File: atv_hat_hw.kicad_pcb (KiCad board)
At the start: 2 copper layers, 84.1 x 83.9 mm, 51 parts, among them J1 GPIO_CONNECTOR, J10 conn_01x02_labeled, J11 conn_01x02_labeled, J12 conn_01x02_labeled, J2 conn_01x02_labeled, J3 conn_01x02_labeled, J4 conn_01x02_labeled, J5 conn_01x02_labeled, J6 conn_01x02_labeled, J7 enc28j60_hanrun, J8 conn_01x02_labeled, J9 conn_01x02_labeled, Q1 Q_NMOS_GDS, Q2 Q_NMOS_GDS, Q3 Q_NMOS_GDS, Q4 Q_NMOS_GDS, Q5 Q_NMOS_GDS, Q6 Q_NMOS_GDS, Q7 Q_NMOS_GDS, Q8 Q_NMOS_GDS, Q9 Q_NMOS_GDS

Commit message: plus board ready for routing
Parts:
- removed D7, D8: Green, LED_SMD:LED_1206_3216Metric_Pad1.42x1.75mm_HandSolder
- removed the H4 at (90.6, 129.6)
- added C10: 10u, Capacitor_SMD:C_1206_3216Metric_Pad1.42x1.75mm_HandSolder, F.Cu at (80.0, 107.9)
- added C11: 100n, Capacitor_SMD:C_1206_3216Metric_Pad1.42x1.75mm_HandSolder, F.Cu at (90.6, 37.8)
- added C12: 30p, Capacitor_SMD:C_1206_3216Metric_Pad1.42x1.75mm_HandSolder, F.Cu at (86.0, 43.3)
- added C13: 30p, Capacitor_SMD:C_1206_3216Metric_Pad1.42x1.75mm_HandSolder, F.Cu at (90.6, 34.5)
- added C14: 10u, Capacitor_SMD:C_1206_3216Metric_Pad1.42x1.75mm_HandSolder, F.Cu at (80.1, 46.6)
- added C15: 100n, Capacitor_SMD:C_1206_3216Metric_Pad1.42x1.75mm_HandSolder, F.Cu at (99.2, 24.6)
- added C16: 100n, Capacitor_SMD:C_1206_3216Metric_Pad1.42x1.75mm_HandSolder, F.Cu at (90.6, 31.2)
- added C17: 10u, Capacitor_SMD:C_1206_3216Metric_Pad1.42x1.75mm_HandSolder, F.Cu at (93.2, 27.9)
- added C3: 100n, Capacitor_SMD:C_1206_3216Metric_Pad1.42x1.75mm_HandSolder, F.Cu at (82.4, 66.4)
- added C4: 10u, Capacitor_SMD:C_1206_3216Metric_Pad1.42x1.75mm_HandSolder, F.Cu at (78.7, 61.8)
- added C5: 100n, Capacitor_SMD:C_1206_3216Metric_Pad1.42x1.75mm_HandSolder, F.Cu at (96.0, 75.4)
- added C6: 10u, Capacitor_SMD:C_1206_3216Metric_Pad1.42x1.75mm_HandSolder, F.Cu at (95.5, 84.3)
- added C7: 100n, Capacitor_SMD:C_1206_3216Metric_Pad1.42x1.75mm_HandSolder, F.Cu at (97.8, 98.4)
- added C8: 10u, Capacitor_SMD:C_1206_3216Metric_Pad1.42x1.75mm_HandSolder, F.Cu at (98.0, 93.1)
- added C9: 100n, Capacitor_SMD:C_1206_3216Metric_Pad1.42x1.75mm_HandSolder, F.Cu at (80.0, 110.2)
- added FB1: 80mA, Inductor_SMD:L_1206_3216Metric_Pad1.42x1.75mm_HandSolder, F.Cu at (80.1, 43.3)
- added H1: MountingHole, lib:MountingHole_2.7mm_M2.5_uHAT_RPi, F.Cu at (106.3, 23.3)
- added J0: phoenix_1935161, lib:PHOENIX_1935161, F.Cu at (106.0, 64.6)
- added J13: phoenix_1935161, lib:PHOENIX_1935161, F.Cu at (245.1, 64.6)
- added J14: phoenix_1935161, lib:PHOENIX_1935161, F.Cu at (255.8, 64.6)
- added J15: phoenix_1935161, lib:PHOENIX_1935161, F.Cu at (266.4, 64.6)
- added J16: phoenix_1935161, lib:PHOENIX_1935161, F.Cu at (103.8, 81.2)
- added J17: phoenix_1935161, lib:PHOENIX_1935161, F.Cu at (114.9, 81.2)
- added J18: phoenix_1935161, lib:PHOENIX_1935161, F.Cu at (125.6, 81.2)
- added J19: phoenix_1935161, lib:PHOENIX_1935161, F.Cu at (136.3, 81.2)
- added J20: phoenix_1935161, lib:PHOENIX_1935161, F.Cu at (147.2, 81.2)
- added J21: phoenix_1935161, lib:PHOENIX_1935161, F.Cu at (157.9, 81.2)
- added J22: phoenix_1935161, lib:PHOENIX_1935161, F.Cu at (168.5, 81.2)
- added J23: phoenix_1935161, lib:PHOENIX_1935161, F.Cu at (179.5, 81.2)
- added J24: phoenix_1935161, lib:PHOENIX_1935161, F.Cu at (190.4, 81.2)
- added J25: phoenix_1935161, lib:PHOENIX_1935161, F.Cu at (201.3, 81.2)
- added J26: phoenix_1935161, lib:PHOENIX_1935161, F.Cu at (212.2, 81.2)
- added J27: phoenix_1935161, lib:PHOENIX_1935161, F.Cu at (222.9, 81.2)
- added J28: phoenix_1935161, lib:PHOENIX_1935161, F.Cu at (233.8, 81.2)
- added J29: phoenix_1935161, lib:PHOENIX_1935161, F.Cu at (244.5, 81.2)
- added J30: phoenix_1935161, lib:PHOENIX_1935161, F.Cu at (255.1, 81.2)
- added J31: phoenix_1935161, lib:PHOENIX_1935161, F.Cu at (265.8, 81.2)
- added J32: phoenix_1935161, lib:PHOENIX_1935161, F.Cu at (105.3, 97.5)
- added J33: phoenix_1935161, lib:PHOENIX_1935161, F.Cu at (116.0, 97.5)
- added J34: phoenix_1935161, lib:PHOENIX_1935161, F.Cu at (126.6, 97.5)
- added J35: phoenix_1935161, lib:PHOENIX_1935161, F.Cu at (137.3, 97.5)
- added J36: phoenix_1935161, lib:PHOENIX_1935161, F.Cu at (148.0, 97.5)
- added J37: phoenix_1935161, lib:PHOENIX_1935161, F.Cu at (158.6, 97.5)
- added J38: phoenix_1935161, lib:PHOENIX_1935161, F.Cu at (169.3, 97.5)
- added J39: phoenix_1935161, lib:PHOENIX_1935161, F.Cu at (180.0, 97.5)
- added J40: phoenix_1935161, lib:PHOENIX_1935161, F.Cu at (190.6, 97.5)
- added J41: phoenix_1935161, lib:PHOENIX_1935161, F.Cu at (201.3, 97.5)
- added J42: phoenix_1935161, lib:PHOENIX_1935161, F.Cu at (212.0, 97.5)
- added J43: phoenix_1935161, lib:PHOENIX_1935161, F.Cu at (222.6, 97.5)
- added J44: phoenix_1935161, lib:PHOENIX_1935161, F.Cu at (233.3, 97.5)
- added J45: phoenix_1935161, lib:PHOENIX_1935161, F.Cu at (244.0, 97.5)
- added J46: phoenix_1935161, lib:PHOENIX_1935161, F.Cu at (254.6, 97.5)
- added J47: phoenix_1935161, lib:PHOENIX_1935161, F.Cu at (265.3, 97.5)
- added J48: phoenix_1935161, lib:PHOENIX_1935161, F.Cu at (103.5, 117.2)
- added J49: phoenix_1935161, lib:PHOENIX_1935161, F.Cu at (114.2, 117.2)
- added J50: phoenix_1935161, lib:PHOENIX_1935161, F.Cu at (124.8, 117.2)
- added J51: phoenix_1935161, lib:PHOENIX_1935161, F.Cu at (135.5, 117.2)
- added J52: phoenix_1935161, lib:PHOENIX_1935161, F.Cu at (146.2, 117.2)
- added J53: phoenix_1935161, lib:PHOENIX_1935161, F.Cu at (156.8, 117.2)
- added J54: phoenix_1935161, lib:PHOENIX_1935161, F.Cu at (167.5, 117.2)
- added J55: phoenix_1935161, lib:PHOENIX_1935161, F.Cu at (178.2, 117.2)
- added J56: phoenix_1935161, lib:PHOENIX_1935161, F.Cu at (188.8, 117.2)
- added J57: phoenix_1935161, lib:PHOENIX_1935161, F.Cu at (199.5, 117.2)
- added J58: phoenix_1935161, lib:PHOENIX_1935161, F.Cu at (210.2, 117.2)
- added J59: phoenix_1935161, lib:PHOENIX_1935161, F.Cu at (220.9, 117.2)
- added J60: phoenix_1935161, lib:PHOENIX_1935161, F.Cu at (231.5, 117.2)
- added J61: phoenix_1935161, lib:PHOENIX_1935161, F.Cu at (242.3, 117.2)
- added J62: phoenix_1935161, lib:PHOENIX_1935161, F.Cu at (253.0, 117.2)
- added J63: phoenix_1935161, lib:PHOENIX_1935161, F.Cu at (263.7, 117.2)
- added J64: phoenix_1935161, lib:SolderWirePad_1x02_P9.0mm_Drill4.5mm, F.Cu at (56.5, 105.3)
- added J65: GPIO_CONNECTOR, lib:PinSocket_2x20_P2.54mm_Vertical_Centered_Anchor, B.Cu at (135.5, 23.1)
- added P1: RB1-125BAG1A, WIZNET_RB1-125BAG1A, F.Cu at (60.5, 35.1)
- added Q0: Q_NMOS_GSD, Package_TO_SOT_SMD:SOT-23_Handsoldering, F.Cu at (108.6, 58.2)
- added Q10: Q_NMOS_GSD, Package_TO_SOT_SMD:SOT-23_Handsoldering, F.Cu at (215.6, 58.5)
- added Q11: Q_NMOS_GSD, Package_TO_SOT_SMD:SOT-23_Handsoldering, F.Cu at (226.3, 58.5)
- added Q12: Q_NMOS_GSD, Package_TO_SOT_SMD:SOT-23_Handsoldering, F.Cu at (237.0, 58.5)
- added Q13: Q_NMOS_GSD, Package_TO_SOT_SMD:SOT-23_Handsoldering, F.Cu at (247.7, 58.5)
- added Q14: Q_NMOS_GSD, Package_TO_SOT_SMD:SOT-23_Handsoldering, F.Cu at (258.3, 58.5)
- added Q15: Q_NMOS_GSD, Package_TO_SOT_SMD:SOT-23_Handsoldering, F.Cu at (269.0, 58.2)
- added Q16: Q_NMOS_GSD, Package_TO_SOT_SMD:SOT-23_Handsoldering, F.Cu at (106.3, 75.1)
- added Q17: Q_NMOS_GSD, Package_TO_SOT_SMD:SOT-23_Handsoldering, F.Cu at (117.5, 75.1)
- added Q18: Q_NMOS_GSD, Package_TO_SOT_SMD:SOT-23_Handsoldering, F.Cu at (128.1, 75.1)
- added Q19: Q_NMOS_GSD, Package_TO_SOT_SMD:SOT-23_Handsoldering, F.Cu at (138.8, 75.1)
- added Q20: Q_NMOS_GSD, Package_TO_SOT_SMD:SOT-23_Handsoldering, F.Cu at (149.7, 75.1)
- added Q21: Q_NMOS_GSD, Package_TO_SOT_SMD:SOT-23_Handsoldering, F.Cu at (160.4, 75.1)
- added Q22: Q_NMOS_GSD, Package_TO_SOT_SMD:SOT-23_Handsoldering, F.Cu at (171.1, 75.1)
- added Q23: Q_NMOS_GSD, Package_TO_SOT_SMD:SOT-23_Handsoldering, F.Cu at (182.0, 75.1)
- added Q24: Q_NMOS_GSD, Package_TO_SOT_SMD:SOT-23_Handsoldering, F.Cu at (192.9, 74.9)
- added Q25: Q_NMOS_GSD, Package_TO_SOT_SMD:SOT-23_Handsoldering, F.Cu at (203.8, 75.1)
- added Q26: Q_NMOS_GSD, Package_TO_SOT_SMD:SOT-23_Handsoldering, F.Cu at (214.8, 75.1)
- added Q27: Q_NMOS_GSD, Package_TO_SOT_SMD:SOT-23_Handsoldering, F.Cu at (225.4, 75.1)
- added Q28: Q_NMOS_GSD, Package_TO_SOT_SMD:SOT-23_Handsoldering, F.Cu at (236.3, 75.1)
- added Q29: Q_NMOS_GSD, Package_TO_SOT_SMD:SOT-23_Handsoldering, F.Cu at (247.0, 75.1)
- added Q30: Q_NMOS_GSD, Package_TO_SOT_SMD:SOT-23_Handsoldering, F.Cu at (257.7, 75.1)
- added Q31: Q_NMOS_GSD, Package_TO_SOT_SMD:SOT-23_Handsoldering, F.Cu at (268.4, 75.1)
- added Q32: Q_NMOS_GSD, Package_TO_SOT_SMD:SOT-23_Handsoldering, F.Cu at (107.8, 91.4)
- added Q33: Q_NMOS_GSD, Package_TO_SOT_SMD:SOT-23_Handsoldering, F.Cu at (118.5, 91.4)
- added Q34: Q_NMOS_GSD, Package_TO_SOT_SMD:SOT-23_Handsoldering, F.Cu at (129.2, 91.4)
- added Q35: Q_NMOS_GSD, Package_TO_SOT_SMD:SOT-23_Handsoldering, F.Cu at (139.8, 91.4)
- added Q36: Q_NMOS_GSD, Package_TO_SOT_SMD:SOT-23_Handsoldering, F.Cu at (150.5, 91.4)
- added Q37: Q_NMOS_GSD, Package_TO_SOT_SMD:SOT-23_Handsoldering, F.Cu at (161.2, 91.4)
- added Q38: Q_NMOS_GSD, Package_TO_SOT_SMD:SOT-23_Handsoldering, F.Cu at (171.8, 91.4)
- added Q39: Q_NMOS_GSD, Package_TO_SOT_SMD:SOT-23_Handsoldering, F.Cu at (182.5, 91.4)
- added Q40: Q_NMOS_GSD, Package_TO_SOT_SMD:SOT-23_Handsoldering, F.Cu at (193.2, 91.4)
- added Q41: Q_NMOS_GSD, Package_TO_SOT_SMD:SOT-23_Handsoldering, F.Cu at (203.8, 91.4)
- added Q42: Q_NMOS_GSD, Package_TO_SOT_SMD:SOT-23_Handsoldering, F.Cu at (214.5, 91.4)
- added Q43: Q_NMOS_GSD, Package_TO_SOT_SMD:SOT-23_Handsoldering, F.Cu at (225.2, 91.4)
- added Q44: Q_NMOS_GSD, Package_TO_SOT_SMD:SOT-23_Handsoldering, F.Cu at (235.8, 91.4)
- added Q45: Q_NMOS_GSD, Package_TO_SOT_SMD:SOT-23_Handsoldering, F.Cu at (246.5, 91.4)
- added Q46: Q_NMOS_GSD, Package_TO_SOT_SMD:SOT-23_Handsoldering, F.Cu at (257.2, 91.4)
- added Q47: Q_NMOS_GSD, Package_TO_SOT_SMD:SOT-23_Handsoldering, F.Cu at (267.8, 91.4)
- added Q48: Q_NMOS_GSD, Package_TO_SOT_SMD:SOT-23_Handsoldering, F.Cu at (106.0, 111.1)
- added Q49: Q_NMOS_GSD, Package_TO_SOT_SMD:SOT-23_Handsoldering, F.Cu at (116.7, 111.1)
- added Q50: Q_NMOS_GSD, Package_TO_SOT_SMD:SOT-23_Handsoldering, F.Cu at (127.4, 111.1)
- added Q51: Q_NMOS_GSD, Package_TO_SOT_SMD:SOT-23_Handsoldering, F.Cu at (138.1, 111.1)
- added Q52: Q_NMOS_GSD, Package_TO_SOT_SMD:SOT-23_Handsoldering, F.Cu at (148.7, 111.1)
- added Q53: Q_NMOS_GSD, Package_TO_SOT_SMD:SOT-23_Handsoldering, F.Cu at (159.4, 111.1)
- added Q54: Q_NMOS_GSD, Package_TO_SOT_SMD:SOT-23_Handsoldering, F.Cu at (169.9, 111.1)
- added Q55: Q_NMOS_GSD, Package_TO_SOT_SMD:SOT-23_Handsoldering, F.Cu at (180.7, 111.1)
- added Q56: Q_NMOS_GSD, Package_TO_SOT_SMD:SOT-23_Handsoldering, F.Cu at (191.4, 111.0)
- added Q57: Q_NMOS_GSD, Package_TO_SOT_SMD:SOT-23_Handsoldering, F.Cu at (202.1, 111.1)
- added Q58: Q_NMOS_GSD, Package_TO_SOT_SMD:SOT-23_Handsoldering, F.Cu at (212.6, 111.1)
- added Q59: Q_NMOS_GSD, Package_TO_SOT_SMD:SOT-23_Handsoldering, F.Cu at (223.4, 111.0)
- added Q60: Q_NMOS_GSD, Package_TO_SOT_SMD:SOT-23_Handsoldering, F.Cu at (234.1, 111.1)
- added Q61: Q_NMOS_GSD, Package_TO_SOT_SMD:SOT-23_Handsoldering, F.Cu at (244.9, 111.0)
- added Q62: Q_NMOS_GSD, Package_TO_SOT_SMD:SOT-23_Handsoldering, F.Cu at (255.5, 111.1)
- added Q63: Q_NMOS_GSD, Package_TO_SOT_SMD:SOT-23_Handsoldering, F.Cu at (266.2, 111.1)
- added R0: 10k, Resistor_SMD:R_1206_3216Metric_Pad1.42x1.75mm_HandSolder, F.Cu at (103.3, 59.0)
- added R17: 10k, Resistor_SMD:R_1206_3216Metric_Pad1.42x1.75mm_HandSolder, F.Cu at (112.1, 75.6)
- added R18: 10k, Resistor_SMD:R_1206_3216Metric_Pad1.42x1.75mm_HandSolder, F.Cu at (122.8, 75.6)
- added R19: 10k, Resistor_SMD:R_1206_3216Metric_Pad1.42x1.75mm_HandSolder, F.Cu at (133.5, 75.6)
- added R20: 10k, Resistor_SMD:R_1206_3216Metric_Pad1.42x1.75mm_HandSolder, F.Cu at (144.4, 75.6)
- added R21: 10k, Resistor_SMD:R_1206_3216Metric_Pad1.42x1.75mm_HandSolder, F.Cu at (155.1, 75.6)
- added R22: 10k, Resistor_SMD:R_1206_3216Metric_Pad1.42x1.75mm_HandSolder, F.Cu at (165.7, 75.6)
- added R23: 10k, Resistor_SMD:R_1206_3216Metric_Pad1.42x1.75mm_HandSolder, F.Cu at (176.7, 75.6)
- added R24: 10k, Resistor_SMD:R_1206_3216Metric_Pad1.42x1.75mm_HandSolder, F.Cu at (187.6, 75.6)
- added R25: 10k, Resistor_SMD:R_1206_3216Metric_Pad1.42x1.75mm_HandSolder, F.Cu at (198.5, 75.6)
- added R26: 10k, Resistor_SMD:R_1206_3216Metric_Pad1.42x1.75mm_HandSolder, F.Cu at (209.4, 75.6)
- added R27: 10k, Resistor_SMD:R_1206_3216Metric_Pad1.42x1.75mm_HandSolder, F.Cu at (220.1, 75.9)
- added R28: 10k, Resistor_SMD:R_1206_3216Metric_Pad1.42x1.75mm_HandSolder, F.Cu at (231.0, 75.6)
- added R29: 10k, Resistor_SMD:R_1206_3216Metric_Pad1.42x1.75mm_HandSolder, F.Cu at (241.7, 75.6)
- added R30: 10k, Resistor_SMD:R_1206_3216Metric_Pad1.42x1.75mm_HandSolder, F.Cu at (252.3, 75.6)
- added R31: 10k, Resistor_SMD:R_1206_3216Metric_Pad1.42x1.75mm_HandSolder, F.Cu at (263.0, 75.6)
- added R32: 10k, Resistor_SMD:R_1206_3216Metric_Pad1.42x1.75mm_HandSolder, F.Cu at (102.5, 91.9)
- added R33: 10k, Resistor_SMD:R_1206_3216Metric_Pad1.42x1.75mm_HandSolder, F.Cu at (113.2, 91.9)
- added R34: 10k, Resistor_SMD:R_1206_3216Metric_Pad1.42x1.75mm_HandSolder, F.Cu at (123.8, 91.9)
- added R35: 10k, Resistor_SMD:R_1206_3216Metric_Pad1.42x1.75mm_HandSolder, F.Cu at (134.5, 91.9)
- added R36: 10k, Resistor_SMD:R_1206_3216Metric_Pad1.42x1.75mm_HandSolder, F.Cu at (145.2, 91.9)
- added R37: 10k, Resistor_SMD:R_1206_3216Metric_Pad1.42x1.75mm_HandSolder, F.Cu at (155.8, 91.9)
- added R38: 10k, Resistor_SMD:R_1206_3216Metric_Pad1.42x1.75mm_HandSolder, F.Cu at (166.5, 91.9)
- added R39: 10k, Resistor_SMD:R_1206_3216Metric_Pad1.42x1.75mm_HandSolder, F.Cu at (177.2, 91.9)
- added R40: 10k, Resistor_SMD:R_1206_3216Metric_Pad1.42x1.75mm_HandSolder, F.Cu at (187.8, 91.9)
- added R41: 10k, Resistor_SMD:R_1206_3216Metric_Pad1.42x1.75mm_HandSolder, F.Cu at (198.5, 91.9)
- added R42: 10k, Resistor_SMD:R_1206_3216Metric_Pad1.42x1.75mm_HandSolder, F.Cu at (209.2, 91.9)
- added R43: 10k, Resistor_SMD:R_1206_3216Metric_Pad1.42x1.75mm_HandSolder, F.Cu at (219.8, 91.9)
- added R44: 10k, Resistor_SMD:R_1206_3216Metric_Pad1.42x1.75mm_HandSolder, F.Cu at (230.5, 91.9)
- added R45: 10k, Resistor_SMD:R_1206_3216Metric_Pad1.42x1.75mm_HandSolder, F.Cu at (241.2, 91.9)
- added R46: 10k, Resistor_SMD:R_1206_3216Metric_Pad1.42x1.75mm_HandSolder, F.Cu at (251.8, 91.9)
- added R47: 10k, Resistor_SMD:R_1206_3216Metric_Pad1.42x1.75mm_HandSolder, F.Cu at (262.5, 91.9)
- added R48: 10k, Resistor_SMD:R_1206_3216Metric_Pad1.42x1.75mm_HandSolder, F.Cu at (100.7, 111.6)
- added R49: 10k, Resistor_SMD:R_1206_3216Metric_Pad1.42x1.75mm_HandSolder, F.Cu at (111.4, 111.6)
- added R50: 10k, Resistor_SMD:R_1206_3216Metric_Pad1.42x1.75mm_HandSolder, F.Cu at (122.0, 111.6)
- added R51: 10k, Resistor_SMD:R_1206_3216Metric_Pad1.42x1.75mm_HandSolder, F.Cu at (132.7, 111.6)
- added R52: 10k, Resistor_SMD:R_1206_3216Metric_Pad1.42x1.75mm_HandSolder, F.Cu at (143.4, 111.6)
- added R53: 10k, Resistor_SMD:R_1206_3216Metric_Pad1.42x1.75mm_HandSolder, F.Cu at (154.1, 111.6)
- added R54: 10k, Resistor_SMD:R_1206_3216Metric_Pad1.42x1.75mm_HandSolder, F.Cu at (164.7, 111.7)
- added R55: 10k, Resistor_SMD:R_1206_3216Metric_Pad1.42x1.75mm_HandSolder, F.Cu at (175.4, 111.7)
- added R56: 10k, Resistor_SMD:R_1206_3216Metric_Pad1.42x1.75mm_HandSolder, F.Cu at (186.1, 111.6)
- added R57: 10k, Resistor_SMD:R_1206_3216Metric_Pad1.42x1.75mm_HandSolder, F.Cu at (196.7, 111.7)
- added R58: 10k, Resistor_SMD:R_1206_3216Metric_Pad1.42x1.75mm_HandSolder, F.Cu at (207.4, 111.7)
- added R59: 10k, Resistor_SMD:R_1206_3216Metric_Pad1.42x1.75mm_HandSolder, F.Cu at (218.2, 111.6)
- added R60: 10k, Resistor_SMD:R_1206_3216Metric_Pad1.42x1.75mm_HandSolder, F.Cu at (228.7, 111.7)
- added R61: 10k, Resistor_SMD:R_1206_3216Metric_Pad1.42x1.75mm_HandSolder, F.Cu at (239.5, 111.6)
- added R62: 10k, Resistor_SMD:R_1206_3216Metric_Pad1.42x1.75mm_HandSolder, F.Cu at (250.2, 111.6)
- added R63: 10k, Resistor_SMD:R_1206_3216Metric_Pad1.42x1.75mm_HandSolder, F.Cu at (260.9, 111.7)
- added R64: 220, Resistor_SMD:R_1206_3216Metric_Pad1.42x1.75mm_HandSolder, F.Cu at (55.8, 65.0)
- added R65: 10k, Resistor_SMD:R_1206_3216Metric_Pad1.42x1.75mm_HandSolder, F.Cu at (59.1, 76.9)
- added R66: 10k, Resistor_SMD:R_1206_3216Metric_Pad1.42x1.75mm_HandSolder, F.Cu at (59.1, 70.9)
- added R67: 220, Resistor_SMD:R_1206_3216Metric_Pad1.42x1.75mm_HandSolder, F.Cu at (62.4, 76.9)
- added R68: 220, Resistor_SMD:R_1206_3216Metric_Pad1.42x1.75mm_HandSolder, F.Cu at (55.8, 70.9)
- added R69: 220, Resistor_SMD:R_1206_3216Metric_Pad1.42x1.75mm_HandSolder, F.Cu at (52.5, 65.0)
- added R70: 220, Resistor_SMD:R_1206_3216Metric_Pad1.42x1.75mm_HandSolder, F.Cu at (52.5, 59.0)
- added R71: 10k, Resistor_SMD:R_1206_3216Metric_Pad1.42x1.75mm_HandSolder, F.Cu at (84.6, 57.6)
- added R72: 10k, Resistor_SMD:R_1206_3216Metric_Pad1.42x1.75mm_HandSolder, F.Cu at (80.6, 79.3)
- added R73: 10k, Resistor_SMD:R_1206_3216Metric_Pad1.42x1.75mm_HandSolder, F.Cu at (91.4, 57.9)
- added R74: 10k, Resistor_SMD:R_1206_3216Metric_Pad1.42x1.75mm_HandSolder, F.Cu at (83.8, 72.9)
- added R75: 10k, Resistor_SMD:R_1206_3216Metric_Pad1.42x1.75mm_HandSolder, F.Cu at (96.9, 58.1)
- added R76: 10k, Resistor_SMD:R_1206_3216Metric_Pad1.42x1.75mm_HandSolder, F.Cu at (88.8, 73.7)
- added R77: 10k, Resistor_SMD:R_1206_3216Metric_Pad1.42x1.75mm_HandSolder, F.Cu at (73.4, 66.4)
- added R78: 10k, Resistor_SMD:R_1206_3216Metric_Pad1.42x1.75mm_HandSolder, F.Cu at (92.1, 73.1)
- added R79: 10k, Resistor_SMD:R_1206_3216Metric_Pad1.42x1.75mm_HandSolder, F.Cu at (86.4, 90.0)
- added R80: 10k, Resistor_SMD:R_1206_3216Metric_Pad1.42x1.75mm_HandSolder, F.Cu at (88.6, 113.2)
- added R81: 10k, Resistor_SMD:R_1206_3216Metric_Pad1.42x1.75mm_HandSolder, F.Cu at (91.1, 90.6)
- added R82: 10k, Resistor_SMD:R_1206_3216Metric_Pad1.42x1.75mm_HandSolder, F.Cu at (95.4, 112.6)
- added R83: 10k, Resistor_SMD:R_1206_3216Metric_Pad1.42x1.75mm_HandSolder, F.Cu at (93.9, 97.5)
- added R84: 10k, Resistor_SMD:R_1206_3216Metric_Pad1.42x1.75mm_HandSolder, F.Cu at (111.5, 106.1)
- added R85: 10k, Resistor_SMD:R_1206_3216Metric_Pad1.42x1.75mm_HandSolder, F.Cu at (95.0, 91.4)
- added R86: 10k, Resistor_SMD:R_1206_3216Metric_Pad1.42x1.75mm_HandSolder, F.Cu at (92.3, 116.3)
- added R87: 10k, Resistor_SMD:R_1206_3216Metric_Pad1.42x1.75mm_HandSolder, F.Cu at (73.5, 115.0)
- added R88: 10k, Resistor_SMD:R_1206_3216Metric_Pad1.42x1.75mm_HandSolder, F.Cu at (73.4, 117.8)
- added R89: 10k, Resistor_SMD:R_1206_3216Metric_Pad1.42x1.75mm_HandSolder, F.Cu at (93.2, 24.6)
- added R90: 10k, Resistor_SMD:R_1206_3216Metric_Pad1.42x1.75mm_HandSolder, F.Cu at (96.6, 31.2)
- added R91: 10k, Resistor_SMD:R_1206_3216Metric_Pad1.42x1.75mm_HandSolder, F.Cu at (86.0, 46.6)
- added R92: 10k, Resistor_SMD:R_1206_3216Metric_Pad1.42x1.75mm_HandSolder, F.Cu at (92.0, 44.4)
- added R93: 49.9, Resistor_SMD:R_1206_3216Metric_Pad1.42x1.75mm_HandSolder, F.Cu at (97.9, 41.0)
- added R94: 49.9, Resistor_SMD:R_1206_3216Metric_Pad1.42x1.75mm_HandSolder, F.Cu at (99.2, 27.9)
- added R95: 49.9, Resistor_SMD:R_1206_3216Metric_Pad1.42x1.75mm_HandSolder, F.Cu at (96.6, 37.8)
- added R96: 2.32k, Resistor_SMD:R_1206_3216Metric_Pad1.42x1.75mm_HandSolder, F.Cu at (92.0, 41.1)
- added R97: 49.9, Resistor_SMD:R_1206_3216Metric_Pad1.42x1.75mm_HandSolder, F.Cu at (96.6, 34.5)
- added U1: PCA9552PW,118, lib:SOP65P640X110-24N, F.Cu at (90.3, 63.7)
- added U2: PCA9552PW,118, lib:SOP65P640X110-24N, F.Cu at (89.0, 81.7)
- added U3: PCA9552PW,118, lib:SOP65P640X110-24N, F.Cu at (86.1, 98.1)
- added U4: PCA9552PW,118, lib:SOP65P640X110-24N, F.Cu at (81.7, 116.4)
- added U5: ENC28J60x-SS, Package_SO:SSOP-28_5.3x10.2mm_P0.65mm, F.Cu at (82.4, 35.6)
- added Y1: Crystal, Crystal:Crystal_HC49-4H_Vertical, F.Cu at (81.2, 26.3)
- D1: value Blue -> 5.6v; footprint LED_SMD:LED_1206_3216Metric_Pad1.42x1.75mm_HandSolder -> Diode_THT:D_DO-35_SOD27_P7.62mm_Horizontal
- D2: value 5.6v -> Blue; footprint Diode_THT:D_DO-35_SOD27_P7.62mm_Horizontal -> LED_SMD:LED_1206_3216Metric_Pad1.42x1.75mm_HandSolder
- J1: value GPIO_CONNECTOR -> phoenix_1935161; footprint lib:PinSocket_2x20_P2.54mm_Vertical_Centered_Anchor -> lib:PHOENIX_1935161; moved to F.Cu
- J10, J11, J12, J2, J3, J5, J6, J8, J9: value conn_01x02_labeled -> phoenix_1935161; footprint lib:SolderWirePad_1x02_P5.08mm_Drill1.5mm_labeled -> lib:PHOENIX_1935161
- J4: value conn_01x02_labeled -> phoenix_1935161; footprint Connector_Wire:SolderWirePad_1x02_P7.62mm_Drill2.5mm -> lib:PHOENIX_1935161
- J7: value enc28j60_hanrun -> phoenix_1935161; footprint lib:enc28j60_hanrun -> lib:PHOENIX_1935161
- Q1, Q2, Q3, Q4, Q5, Q6, Q7, Q8, Q9: value Q_NMOS_GDS -> Q_NMOS_GSD; footprint lib:SOT230P700X180-3N -> Package_TO_SOT_SMD:SOT-23_Handsoldering
- R1, R10, R2, R4, R5, R6, R7, R8, R9: moved to F.Cu
- R11: value 220 -> 10k
- R12, R13, R14, R15, R16, R3: value 220 -> 10k; moved to F.Cu
- moved R11 139.1 mm to (221.0, 59.0), turned to 180 degrees
- moved R12 137.6 mm to (231.6, 59.0), turned to 180 degrees
- moved R13 135.3 mm to (242.3, 59.0), turned to 180 degrees
- moved R14 133.9 mm to (253.0, 59.0), turned to 180 degrees
- moved R15 131.4 mm to (263.7, 59.0), turned to 180 degrees
- moved C1 99.2 mm to (52.5, 70.9), turned to 90 degrees
- moved C2 97.9 mm to (54.8, 85.1)
- moved D2 95.4 mm to (63.7, 100.8)
- moved D6 92.8 mm to (52.6, 76.8)
- moved D1 88.0 mm to (71.2, 100.4), turned to 90 degrees
- moved J8 78.3 mm to (191.8, 64.6)
- moved J9 77.1 mm to (202.4, 64.6)
- moved J5 75.0 mm to (159.8, 64.6)
- moved J6 74.1 mm to (170.4, 64.6)
- moved D5 72.5 mm to (60.4, 82.8)
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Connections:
- D1 pad 1: GND -> +5V
- D1 pad 2: Net-(D1-Pad2) -> GND
- D2 pad 1: +5V -> GND
- D2 pad 2: GND -> Net-(D2-Pad2)
- J1 pad 1: +3V3 -> GND
- J1 pad 2: +5V -> Net-(J1-Pad2)
- J4 pad 2: +5V -> Net-(J4-Pad2)
- J7 pad 1: +3V3 -> GND
- J7 pad 2: GND -> Net-(J7-Pad2)
- Q1 pad 1: /ATV0_CTRL -> pwr_toggle_01
- Q1 pad 2: +5V -> Net-(J1-Pad2)
- Q1 pad 3: Net-(J2-Pad2) -> +5V
- Q2 pad 1: /ATV1_CTRL -> pwr_toggle_02
- Q2 pad 2: +5V -> Net-(J2-Pad2)
- Q2 pad 3: Net-(J3-Pad2) -> +5V
- Q3 pad 1: /ATV2_CTRL -> pwr_toggle_03
- Q3 pad 2: +5V -> Net-(J3-Pad2)
- Q3 pad 3: Net-(J5-Pad2) -> +5V
- Q4 pad 1: /ATV3_CTRL -> pwr_toggle_04
- Q4 pad 2: +5V -> Net-(J4-Pad2)
- Q4 pad 3: Net-(J6-Pad2) -> +5V
- Q5 pad 1: /ATV4_CTRL -> pwr_toggle_05
- Q5 pad 2: +5V -> Net-(J5-Pad2)
- Q5 pad 3: Net-(J8-Pad2) -> +5V
- Q6 pad 1: /ATV5_CTRL -> pwr_toggle_06
- Q6 pad 2: +5V -> Net-(J6-Pad2)
- Q6 pad 3: Net-(J9-Pad2) -> +5V
- Q7 pad 1: /FAN0_PWM -> pwr_toggle_07
- Q7 pad 2: +5V -> Net-(J7-Pad2)
- Q7 pad 3: Net-(J10-Pad2) -> +5V
- Q8 pad 1: /FAN1_PWM -> pwr_toggle_08
- Q8 pad 2: +5V -> Net-(J8-Pad2)
- Q8 pad 3: Net-(J11-Pad2) -> +5V
- Q9 pad 1: /FAN2_PWM -> pwr_toggle_09
- Q9 pad 2: +5V -> Net-(J9-Pad2)
- Q9 pad 3: Net-(J12-Pad2) -> +5V
- R1 pad 1: +3V3 -> pwr_toggle_01
- R1 pad 2: /ATV0_CTRL -> +3V3
- R10 pad 1: +3V3 -> pwr_toggle_10
- R10 pad 2: /FAN2_PWM -> +3V3
- R11 pad 1: /GPIO23_GEN4 -> pwr_toggle_11
- R11 pad 2: Net-(D3-Pad2) -> +3V3
- R12 pad 1: /GPIO24_GEN5 -> pwr_toggle_12
- R12 pad 2: Net-(D4-Pad2) -> +3V3
- R13 pad 1: /GPIO12 -> pwr_toggle_13
- R13 pad 2: Net-(D5-Pad2) -> +3V3
- R14 pad 1: /GPIO16 -> pwr_toggle_14
- R14 pad 2: Net-(D6-Pad2) -> +3V3
- R15 pad 1: /GPIO20 -> pwr_toggle_15
- R15 pad 2: Net-(D7-Pad2) -> +3V3
- R16 pad 1: /GPIO21 -> pwr_toggle_16
- R16 pad 2: Net-(D8-Pad2) -> +3V3
- R2 pad 1: +3V3 -> pwr_toggle_02
- R2 pad 2: /ATV1_CTRL -> +3V3
- R3 pad 1: +5V -> pwr_toggle_03
- R3 pad 2: Net-(D1-Pad2) -> +3V3
- R4 pad 1: +3V3 -> pwr_toggle_04
- R4 pad 2: /ATV2_CTRL -> +3V3
- R5 pad 1: +3V3 -> pwr_toggle_05
- R5 pad 2: /ATV3_CTRL -> +3V3
- R6 pad 1: +3V3 -> pwr_toggle_06
- R6 pad 2: /ATV4_CTRL -> +3V3
- R7 pad 1: +3V3 -> pwr_toggle_07
- R7 pad 2: /ATV5_CTRL -> +3V3
- R8 pad 1: +3V3 -> pwr_toggle_08
- R8 pad 2: /FAN0_PWM -> +3V3
- R9 pad 1: +3V3 -> pwr_toggle_09
- R9 pad 2: /FAN1_PWM -> +3V3
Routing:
- net +3V3: track 273.9 -> 0.00 mm, vias 10 -> 0
- net +5V: track 268.1 -> 0.00 mm
- net /ATV5_CTRL: track 90.4 -> 0.00 mm, vias 4 -> 0
- net /ATV4_CTRL: track 86.7 -> 0.00 mm, vias 8 -> 0
- net /ATV1_CTRL: track 84.8 -> 0.00 mm, vias 4 -> 0
- net /FAN0_PWM: track 83.4 -> 0.00 mm, vias 2 -> 0
- net /ATV0_CTRL: track 80.5 -> 0.00 mm, vias 3 -> 0
- net /GPIO12: track 77.4 -> 0.00 mm, vias 4 -> 0
- net /ATV2_CTRL: track 75.7 -> 0.00 mm, vias 6 -> 0
- net /GPIO23_GEN4: track 75.6 -> 0.00 mm, vias 2 -> 0
- net /ATV3_CTRL: track 73.3 -> 0.00 mm, vias 6 -> 0
- net /GPIO21: track 73.0 -> 0.00 mm, vias 4 -> 0
- net /FAN1_PWM: track 71.3 -> 0.00 mm, vias 1 -> 0
- net /GPIO24_GEN5: track 69.7 -> 0.00 mm, vias 3 -> 0
- net /GPIO20: track 69.3 -> 0.00 mm, vias 4 -> 0
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- removed copper zone on B.Cu, net GND
- removed copper zone on F.Cu, net GND
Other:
- board size 84.1 x 83.9 mm -> 224.9 x 103.9 mm
- board text added: "- 5v60A +"
- board text added: "ATV Cluster Power Ctrl 64"
- board text removed: "- 5v10A +"
- board text removed: "ATV Cluster Power Ctrl"

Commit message: 64 port hat
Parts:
- removed H1, H3, H4: MountingHole, lib:MountingHole_2.7mm_M2.5_uHAT_RPi
- removed the H2 at (164.5, 23.1)
- added H2: MountingHole, lib:MountingHole_2.7mm_M2.5_uHAT_RPi, F.Cu at (73.9, 25.0)
- added H2: MountingHole, lib:MountingHole_2.7mm_M2.5_uHAT_RPi, F.Cu at (210.8, 25.0)
- added H2: MountingHole, lib:MountingHole_2.7mm_M2.5_uHAT_RPi, F.Cu at (228.7, 132.7)
- added H2: MountingHole, lib:MountingHole_2.7mm_M2.5_uHAT_RPi, F.Cu at (71.0, 152.4)
- added H2: MountingHole, lib:MountingHole_2.7mm_M2.5_uHAT_RPi, F.Cu at (107.4, 154.6)
- C1, C11, C12, C13, C15, R64, R67, R68, R69, R70, R71, R72, R73, R74, R75, R76, R77, R78, R79, R80, R81, R82, R83, R84, R85, R86, R89, R90, R91, U5: moved to B.Cu
- moved P1 189.5 mm to (212.6, 148.2), turned to 90 degrees
- moved Q15 189.4 mm to (81.7, 29.6), turned to 90 degrees
- moved R15 183.4 mm to (81.7, 35.8), turned to 270 degrees
- moved J15 180.2 mm to (89.2, 31.9), turned to 90 degrees
- moved Q14 177.3 mm to (81.7, 42.0), turned to 90 degrees
- moved R14 171.6 mm to (81.7, 48.2), turned to 270 degrees
- moved J14 167.8 mm to (89.2, 44.4), turned to 90 degrees
- moved Q13 166.0 mm to (81.7, 54.4), turned to 90 degrees
- moved R90 165.0 mm to (205.6, 155.1)
- moved R13 160.6 mm to (81.7, 60.7), turned to 270 degrees
- moved R70 159.5 mm to (210.3, 82.9), turned to 0 degrees
- moved R94 158.6 mm to (198.7, 151.4)
- moved C11 158.5 mm to (198.7, 153.8)
- moved D6 157.8 mm to (210.3, 82.9), turned to 0 degrees
- moved Y1 157.7 mm to (173.7, 154.1)
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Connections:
- J65 pad 12: /GPIO18_GEN1 -> GPIO_RST_3
- J65 pad 13: /GPIO27_GEN2 -> GPIO_RST_2
- J65 pad 19: /GPIO10_SPI_MOSI -> GPIO10_SPI_MOSI
- J65 pad 21: /GPIO9_SPI_MISO -> GPIO9_SPI_MISO
- J65 pad 22: /GPIO25_GEN6 -> GPIO25_GEN6
- J65 pad 23: /GPIO11_SPI_SCLK -> GPIO11_SPI_SCLK
- J65 pad 24: /GPIO8_SPI_CE0_N -> GPIO8_SPI_CE0_N
- J65 pad 3: /SDA -> SDA
- J65 pad 33: /GPIO13 -> GPIO_RST_1
- J65 pad 37: /GPIO26 -> GPIO_RST_0
- J65 pad 5: /SCL -> SCL
- R65 pad 1: /SCL -> SCL
- R66 pad 1: /SDA -> SDA
- R67 pad 1: /GPIO12 -> /GPIO21
- R68 pad 1: /GPIO16 -> /GPIO19
- R69 pad 1: /GPIO20 -> /GPIO22_GEN3
- R70 pad 1: /GPIO21 -> /GPIO17_GEN0
- R77 pad 2: /gpio_exp_led/GPIO17_GEN0 -> GPIO_RST_0
- R78 pad 2: /gpio_exp_led/GPIO18_GEN1 -> GPIO_RST_1
- R85 pad 2: /gpio_exp_led/GPIO27_GEN2 -> GPIO_RST_2
- R86 pad 2: /gpio_exp_led/GPIO22_GEN3 -> GPIO_RST_3
- R87 pad 1: /gpio_exp_led/SDA -> SDA
- R88 pad 1: /gpio_exp_led/SCL -> SCL
- R92 pad 2: /ethernet/GPIO8_SPI_CE0_N -> GPIO8_SPI_CE0_N
- U1 pad 10: pwr_toggle_06 -> pwr_toggle_01
- U1 pad 11: pwr_toggle_07 -> pwr_toggle_00
- U1 pad 21: /gpio_exp_led/GPIO17_GEN0 -> GPIO_RST_0
- U1 pad 22: /gpio_exp_led/SCL -> SCL
- U1 pad 23: /gpio_exp_led/SDA -> SDA
- U1 pad 4: pwr_toggle_00 -> pwr_toggle_07
- U1 pad 5: pwr_toggle_01 -> pwr_toggle_06
- U1 pad 6: pwr_toggle_02 -> pwr_toggle_05
- U1 pad 7: pwr_toggle_03 -> pwr_toggle_04
- U1 pad 8: pwr_toggle_04 -> pwr_toggle_03
- U1 pad 9: pwr_toggle_05 -> pwr_toggle_02
- U2 pad 10: pwr_toggle_22 -> pwr_toggle_17
- U2 pad 11: pwr_toggle_23 -> pwr_toggle_16
- U2 pad 21: /gpio_exp_led/GPIO18_GEN1 -> GPIO_RST_1
- U2 pad 22: /gpio_exp_led/SCL -> SCL
- U2 pad 23: /gpio_exp_led/SDA -> SDA
- U2 pad 4: pwr_toggle_16 -> pwr_toggle_23
- U2 pad 5: pwr_toggle_17 -> pwr_toggle_22
- U2 pad 6: pwr_toggle_18 -> pwr_toggle_21
- U2 pad 7: pwr_toggle_19 -> pwr_toggle_20
- U2 pad 8: pwr_toggle_20 -> pwr_toggle_19
- U2 pad 9: pwr_toggle_21 -> pwr_toggle_18
- U3 pad 10: pwr_toggle_38 -> pwr_toggle_33
- U3 pad 11: pwr_toggle_39 -> pwr_toggle_32
- U3 pad 21: /gpio_exp_led/GPIO27_GEN2 -> GPIO_RST_2
- U3 pad 22: /gpio_exp_led/SCL -> SCL
- U3 pad 23: /gpio_exp_led/SDA -> SDA
- U3 pad 4: pwr_toggle_32 -> pwr_toggle_39
- U3 pad 5: pwr_toggle_33 -> pwr_toggle_38
- U3 pad 6: pwr_toggle_34 -> pwr_toggle_37
- U3 pad 7: pwr_toggle_35 -> pwr_toggle_36
- U3 pad 8: pwr_toggle_36 -> pwr_toggle_35
- U3 pad 9: pwr_toggle_37 -> pwr_toggle_34
- U4 pad 10: pwr_toggle_54 -> pwr_toggle_49
- U4 pad 11: pwr_toggle_55 -> pwr_toggle_48
- U4 pad 21: /gpio_exp_led/GPIO22_GEN3 -> GPIO_RST_3
- U4 pad 22: /gpio_exp_led/SCL -> SCL
- U4 pad 23: /gpio_exp_led/SDA -> SDA
- U4 pad 4: pwr_toggle_48 -> pwr_toggle_55
- U4 pad 5: pwr_toggle_49 -> pwr_toggle_54
- U4 pad 6: pwr_toggle_50 -> pwr_toggle_53
- U4 pad 7: pwr_toggle_51 -> pwr_toggle_52
- U4 pad 8: pwr_toggle_52 -> pwr_toggle_51
- U4 pad 9: pwr_toggle_53 -> pwr_toggle_50
- U5 pad 4: /ethernet/GPIO25_GEN6 -> GPIO25_GEN6
- U5 pad 6: /ethernet/GPIO9_SPI_MISO -> GPIO9_SPI_MISO
- U5 pad 7: /ethernet/GPIO10_SPI_MOSI -> GPIO10_SPI_MOSI
- U5 pad 8: /ethernet/GPIO11_SPI_SCLK -> GPIO11_SPI_SCLK
- U5 pad 9: /ethernet/GPIO8_SPI_CE0_N -> GPIO8_SPI_CE0_N
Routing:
- net +3V3: track 0.00 -> 1586.8 mm, vias 0 -> 21
- net SDA: track 0.00 -> 526.9 mm, vias 0 -> 19
- net SCL: track 0.00 -> 455.0 mm, vias 0 -> 18
- net GPIO_RST_3: track 0.00 -> 134.4 mm, vias 0 -> 5
- net GPIO_RST_0: track 0.00 -> 118.1 mm, vias 0 -> 3
- net /GPIO17_GEN0: track 0.00 -> 116.6 mm, vias 0 -> 5
- net /GPIO21: track 0.00 -> 102.1 mm, vias 0 -> 3
- net GPIO_RST_2: track 0.00 -> 95.3 mm, vias 0 -> 5
- net /GPIO19: track 0.00 -> 88.6 mm, vias 0 -> 4
- net GPIO_RST_1: track 0.00 -> 86.6 mm, vias 0 -> 4
- net /GPIO22_GEN3: track 0.00 -> 78.5 mm, vias 0 -> 5
- net GPIO8_SPI_CE0_N: track 0.00 -> 71.1 mm, vias 0 -> 1
- net GPIO11_SPI_SCLK: track 0.00 -> 62.9 mm, vias 0 -> 1
- net GPIO25_GEN6: track 0.00 -> 60.0 mm, vias 0 -> 1
- net GPIO9_SPI_MISO: track 0.00 -> 59.1 mm
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- added copper zone on B.Cu, net +5V
- added copper zone on F.Cu, net +5V
- added copper zone on B.Cu, net GND
- added copper zone on F.Cu, net GND
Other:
- board size 224.9 x 103.9 mm -> 198.5 x 146.7 mm
- board text added: "- 5v 64A +"
- board text added: "Remote Power Ccontrol 64"
- board text removed: "- 5v60A +"
- board text removed: "ATV Cluster Power Ctrl 64"

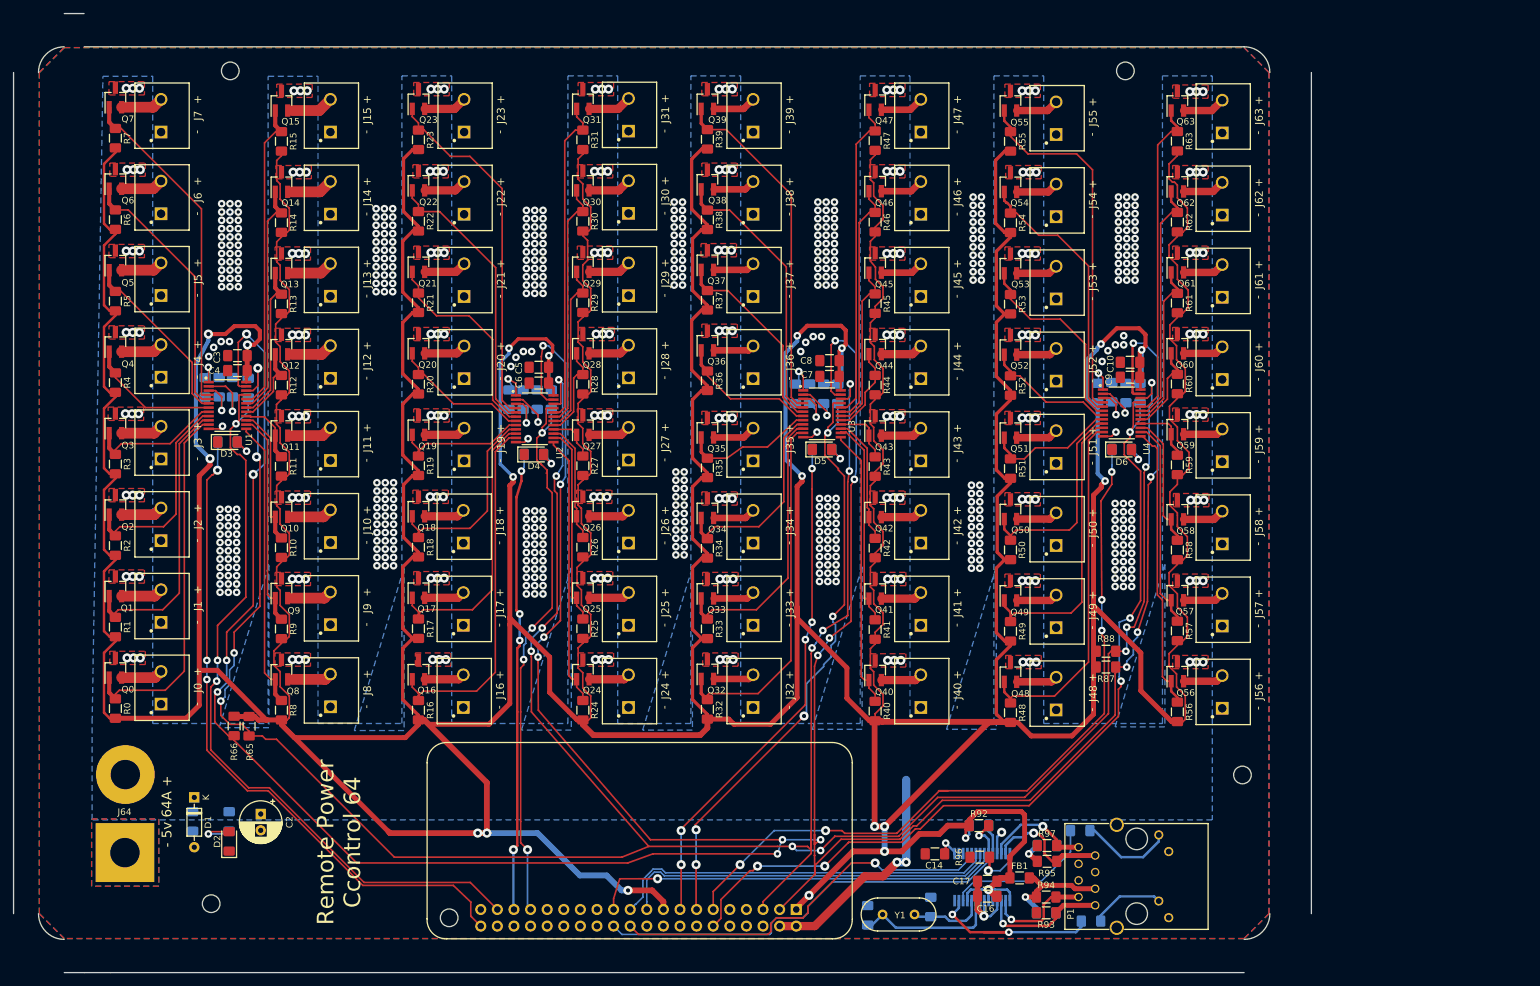
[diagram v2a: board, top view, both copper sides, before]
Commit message: PCB routed for 48 ports
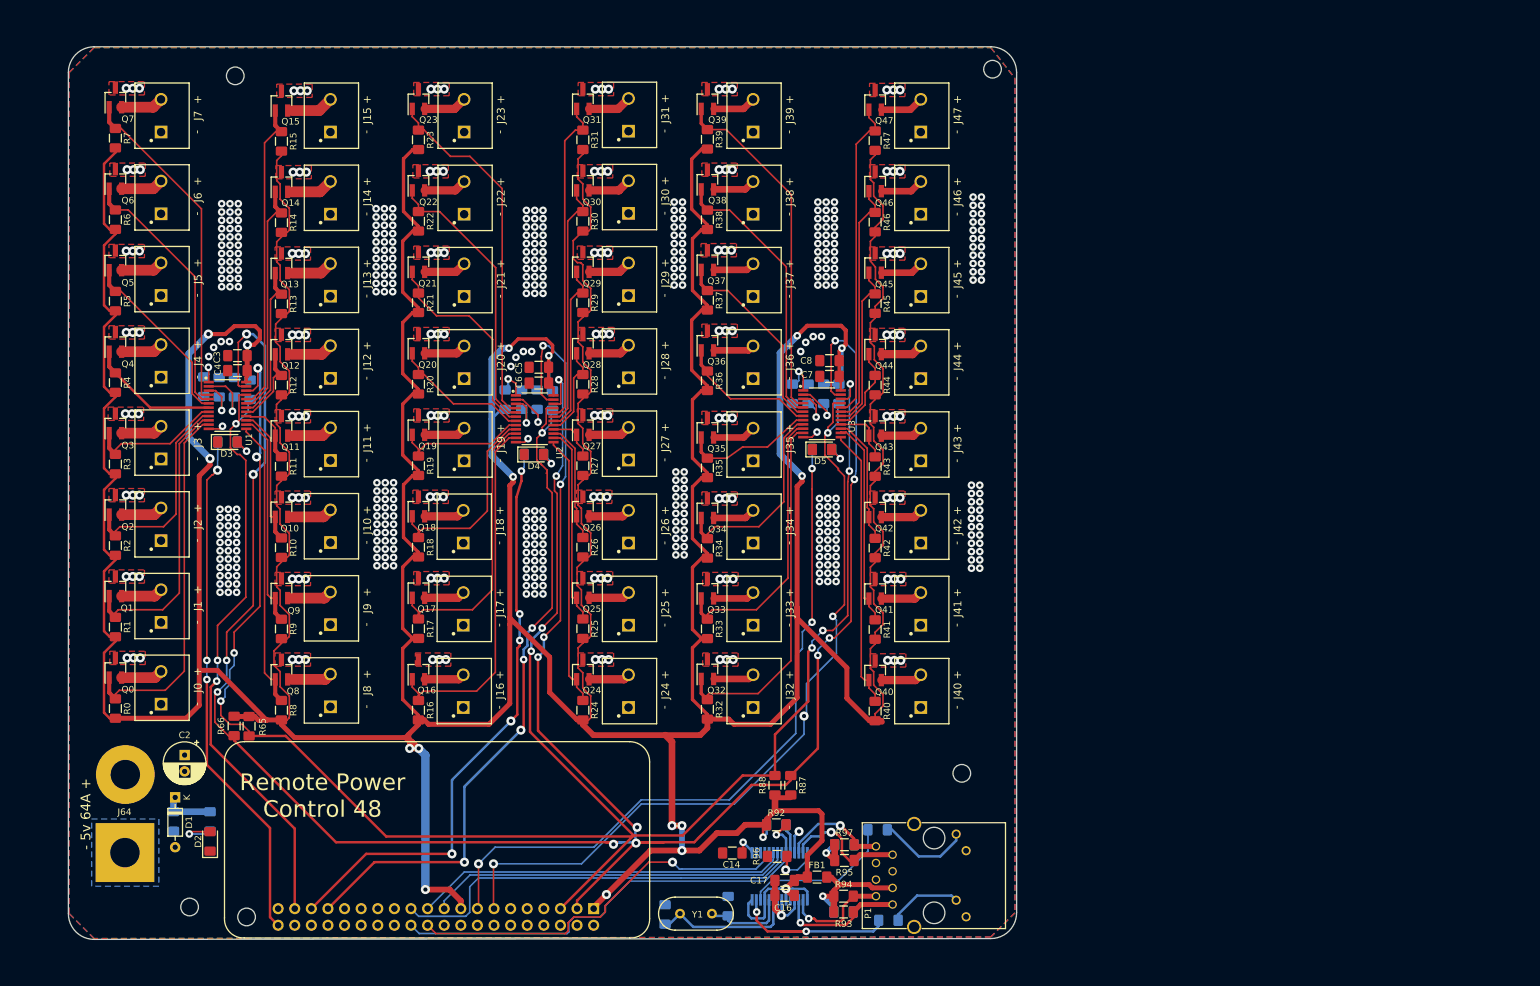
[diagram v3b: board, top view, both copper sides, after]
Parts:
- removed C10: 10u, Capacitor_SMD:C_1206_3216Metric_Pad1.42x1.75mm_HandSolder
- removed C9: 100n, Capacitor_SMD:C_1206_3216Metric_Pad1.42x1.75mm_HandSolder
- removed D6: Green, LED_SMD:LED_1206_3216Metric_Pad1.42x1.75mm_HandSolder
- removed J48, J49, J50, J51, J52, J53, J54, J55, J56, J57, J58, J59, J60, J61, J62, J63: phoenix_1935161, lib:PHOENIX_1935161
- removed Q48, Q49, Q50, Q51, Q52, Q53, Q54, Q55, Q56, Q57, Q58, Q59, Q60, Q61, Q62, Q63: Q_NMOS_GSD, Package_TO_SOT_SMD:SOT-23_Handsoldering
- removed R48, R49, R50, R51, R52, R53, R54, R55, R56, R57, R58, R59, R60, R61, R62, R63, R80, R82, R84, R86: 10k, Resistor_SMD:R_1206_3216Metric_Pad1.42x1.75mm_HandSolder
- removed R70: 220, Resistor_SMD:R_1206_3216Metric_Pad1.42x1.75mm_HandSolder
- removed U4: PCA9552PW,118, lib:SOP65P640X110-24N
- moved R88 54.6 mm to (157.2, 134.3), turned to 270 degrees
- moved R87 51.5 mm to (159.6, 134.3), turned to 270 degrees
- moved H2 42.9 mm to (185.8, 132.5)
- moved C11 31.0 mm to (167.7, 153.7)
- moved C12 31.0 mm to (140.4, 154.1)
- moved C13 31.0 mm to (150.1, 152.8)
- moved C14 31.0 mm to (150.7, 144.7)
- moved C15 31.0 mm to (167.8, 143.4)
- moved C16 31.0 mm to (158.7, 151.1)
- moved C17 31.0 mm to (158.7, 148.8)
- moved FB1 31.0 mm to (163.7, 148.3)
- moved H2 31.0 mm to (76.4, 154.4)
- moved J65 31.0 mm to (105.4, 154.4)
- moved P1 31.0 mm to (181.6, 148.1)
- moved R89 31.0 mm to (157.4, 140.3)
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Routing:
- net +3V3: track 1586.8 -> 1171.5 mm, vias 21 -> 18
- net GPIO_RST_3: track 134.4 -> 0.00 mm, vias 5 -> 0
- net SCL: track 455.0 -> 326.2 mm, vias 18 -> 12
- net /GPIO17_GEN0: track 116.6 -> 0.00 mm, vias 5 -> 0
- net SDA: track 526.9 -> 417.3 mm, vias 19 -> 15
- net pwr_toggle_55: track 55.8 -> 0.00 mm
- net pwr_toggle_48: track 54.5 -> 0.00 mm
- net pwr_toggle_63: track 49.2 -> 0.00 mm
- net pwr_toggle_49: track 44.8 -> 0.00 mm
- net pwr_toggle_56: track 43.8 -> 0.00 mm
- net pwr_toggle_54: track 41.9 -> 0.00 mm
- net pwr_toggle_62: track 37.4 -> 0.00 mm
- net pwr_toggle_57: track 32.2 -> 0.00 mm
- net pwr_toggle_50: track 31.9 -> 0.00 mm
- net pwr_toggle_53: track 30.5 -> 0.00 mm
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- added copper zone on In1.Cu, net +5V
- added copper zone on In2.Cu, net +5V
- removed copper zone on B.Cu, net +5V
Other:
- board size 198.5 x 146.7 mm -> 145 x 136.5 mm
- copper layers 2 -> 4
- board text added: "Remote Power Control 48"
- board text removed: "Remote Power Ccontrol 64"
